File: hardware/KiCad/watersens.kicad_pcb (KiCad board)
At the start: 2 copper layers, 146.1 x 53.3 mm, 77 parts, among them P1 BNC, P2 BNC, P3 BNC, P4 BNC, SW1 SW_PUSH

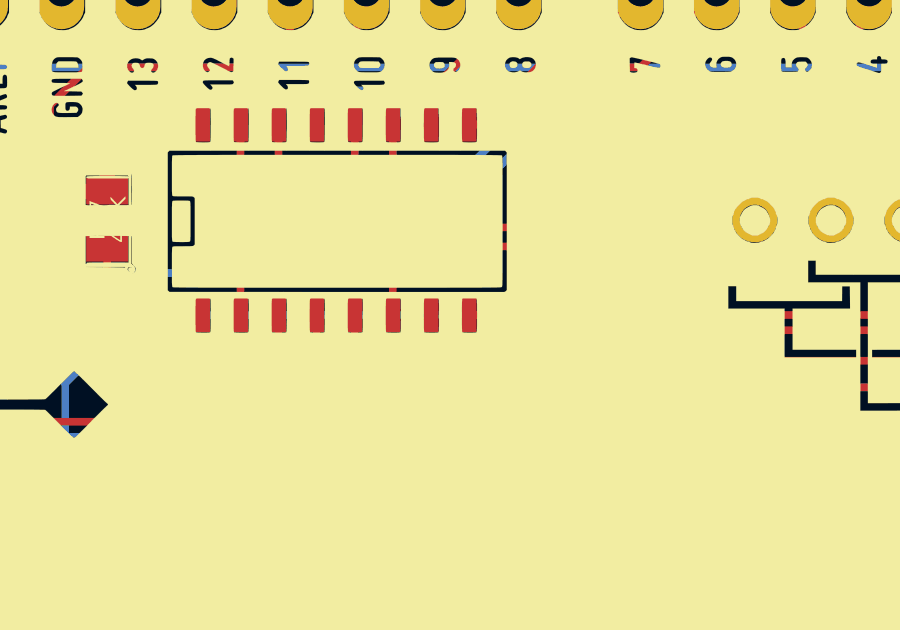
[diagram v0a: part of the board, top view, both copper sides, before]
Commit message: short pin 7 on mux to ground.
update schematic, netlist, PCB, fills, and plots.
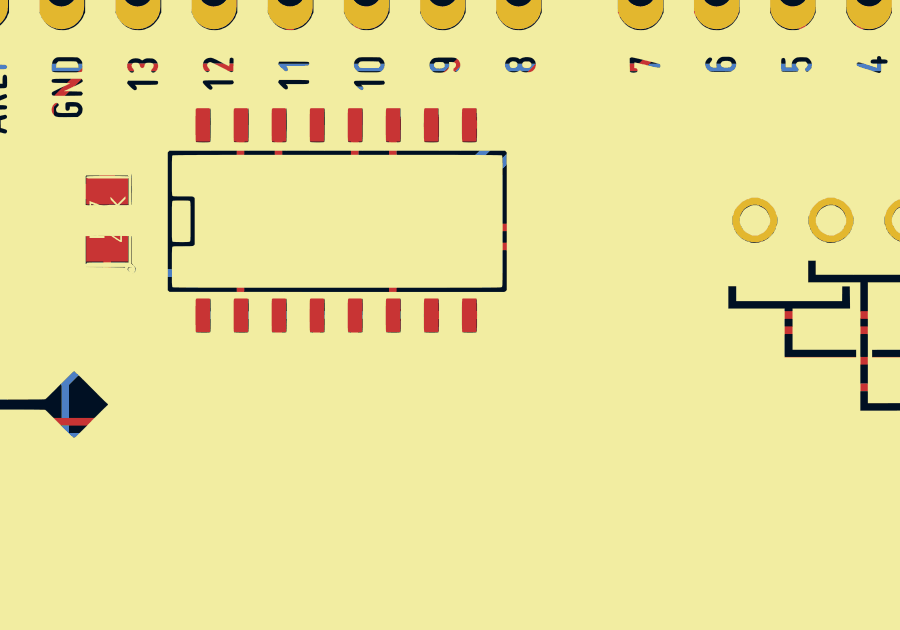
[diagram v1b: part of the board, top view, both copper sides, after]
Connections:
- MUX1 pad 7: (no net) -> GND
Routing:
- net GND: track 429.6 -> 430.8 mm

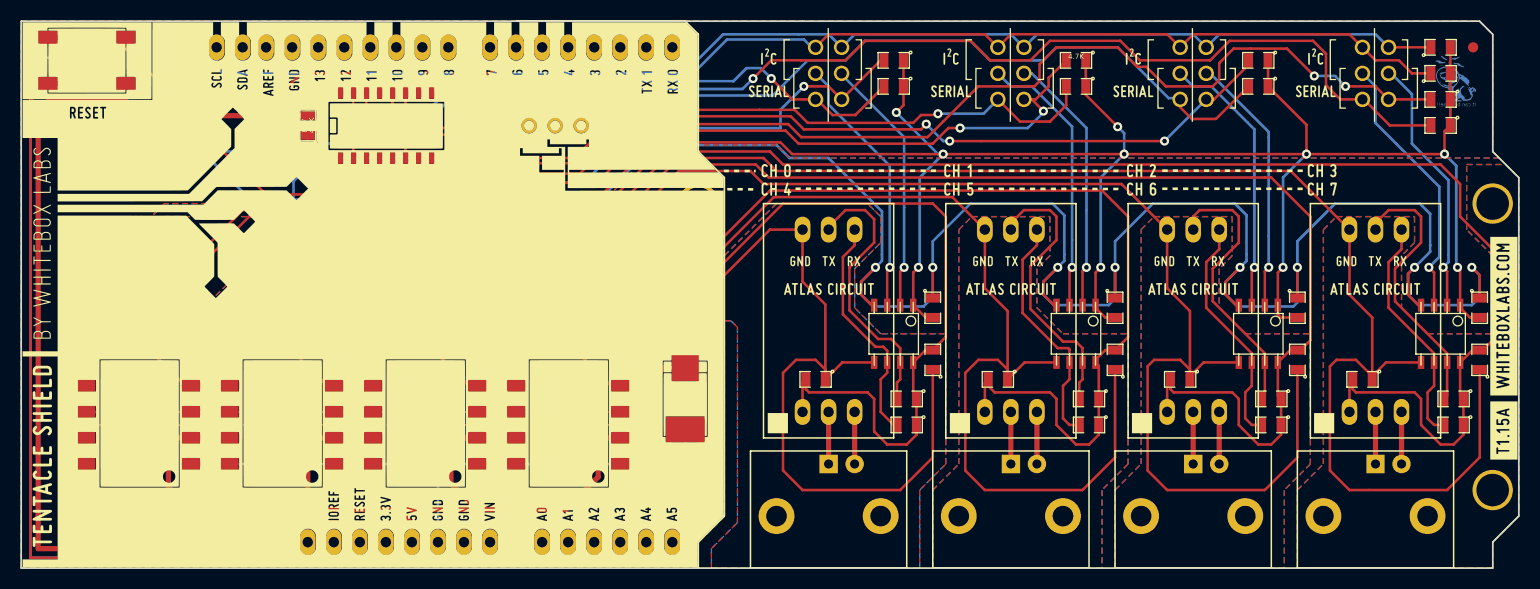
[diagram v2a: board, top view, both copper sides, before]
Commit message: T1.16
added art, removed edges from shield mod SilkS, added previews
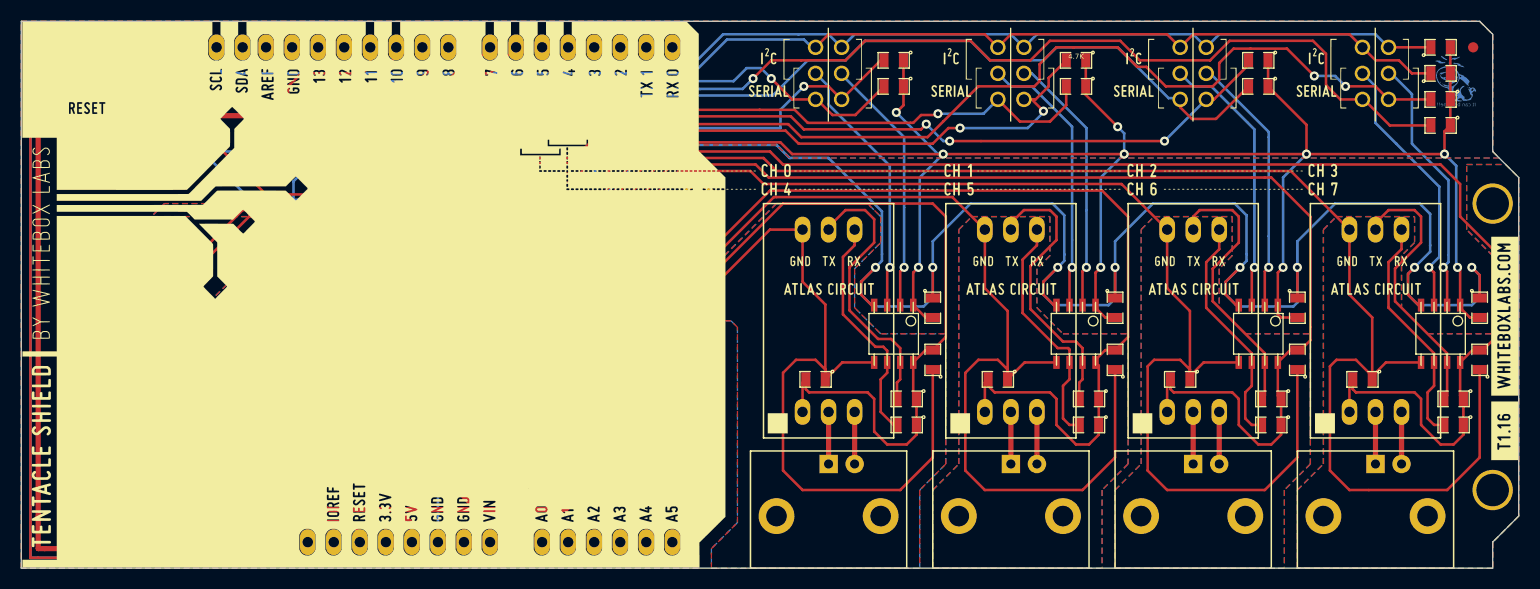
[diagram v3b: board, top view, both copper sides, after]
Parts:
- SHIELD1: footprint ARDUINO_SHIELD_040pinsa -> ARDUINO_SHIELD_040pinsa_no_outline
- moved VAL 0.09 mm to (149.3, 94.0)
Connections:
- MUX1 pad 7: GND -> (no net)

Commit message: removed silkscreen from components
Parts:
- C1, C10, C11, C14, C15, C16, C19, C20, C4, C5, C6, C9, R1, R10, R11, R12, R13, R14, R15, R16, R18, R19, R2, R3, R4, R5, R6, R7, R8, R9: footprint SM0805 -> SM0805a
- P1, P2, P3, P4: footprint BNC-1337543 -> BNC-1337543a
- SIG_ISO1, SIG_ISO2, SIG_ISO3, SIG_ISO4: footprint so-8 -> so-8a
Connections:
- MUX1 pad 7: (no net) -> GND
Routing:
- net GND: track 430.8 -> 429.6 mm
